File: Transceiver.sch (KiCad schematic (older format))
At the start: 31 parts

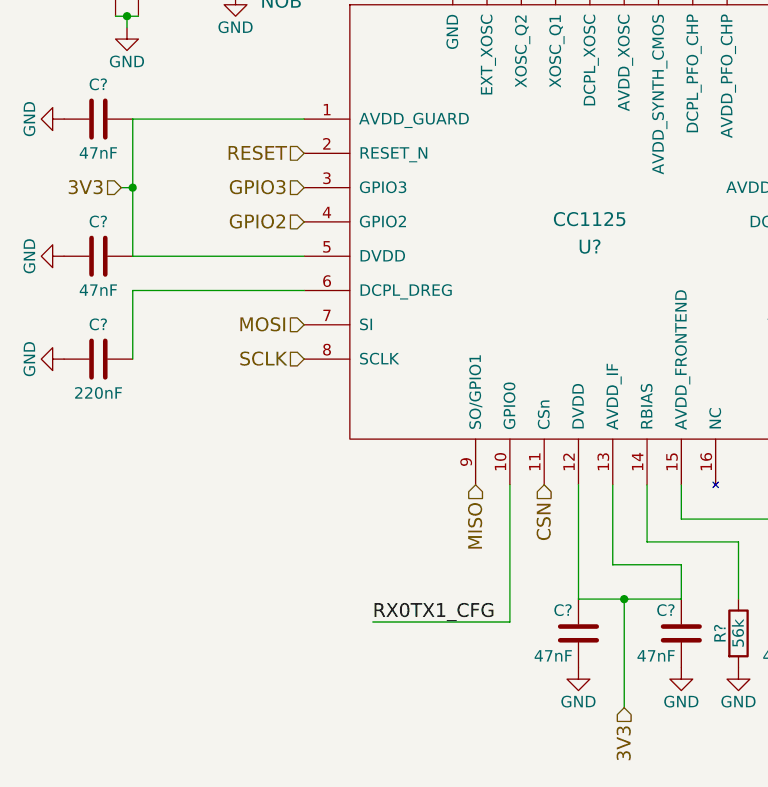
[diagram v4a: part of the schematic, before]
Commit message: added switches for various option and nmos array to control status leds
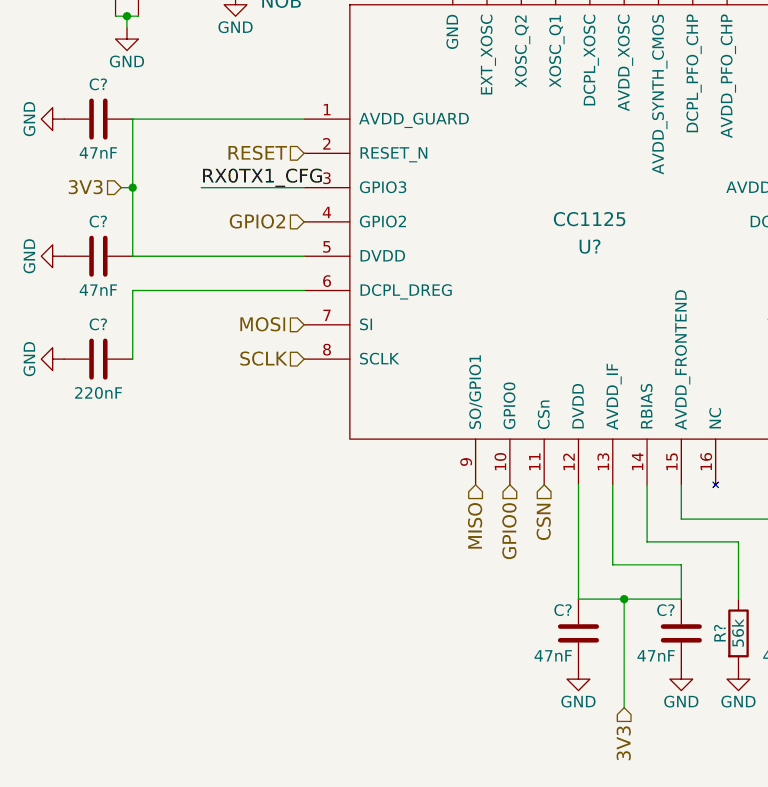
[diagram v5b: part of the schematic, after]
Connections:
- net GPIO3 is gone; now on net TRX_SIG: U?.3 (GPIO3)
- net TRX_SIG: no longer U?.10 (GPIO0)
- new net GPIO0: U?.10 (GPIO0)
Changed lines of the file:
@@
 Text HLabel 1800 3150 0    60   Input ~ 0
 RESET
-Text HLabel 1800 3300 0    60   Input ~ 0
-GPIO3
 Text HLabel 1800 3450 0    60   Input ~ 0
 GPIO2
@@
 Wire Wire Line
 	2350 1350 1850 1350
-Wire Wire Line
-	2700 4600 2700 5200
-Wire Wire Line
-	2700 5200 2100 5200
-Text Label 2100 5200 0    60   ~ 0
+Text Label 1350 3300 0    60   ~ 0
 RX0TX1_CFG
 Text Label 5750 1000 0    60   ~ 0
@@
 Text Label 7800 3200 0    60   ~ 0
 RX0TX1_CFG
+Text HLabel 2700 4600 3    60   Input ~ 0
+GPIO0
+Wire Wire Line
+	1800 3300 1350 3300
 $EndSCHEMATC

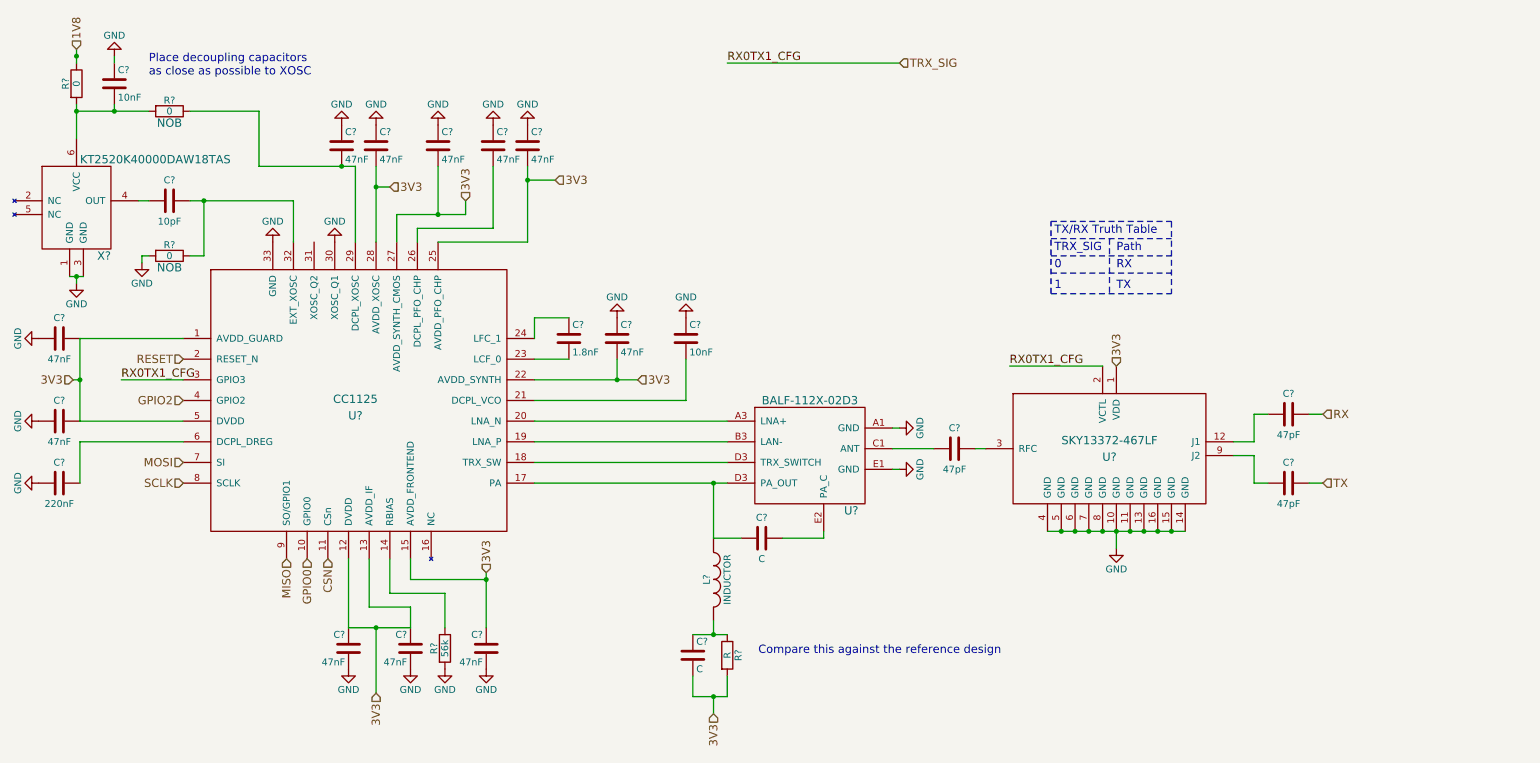
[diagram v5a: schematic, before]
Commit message: added a bunch of footprints and generated layout file
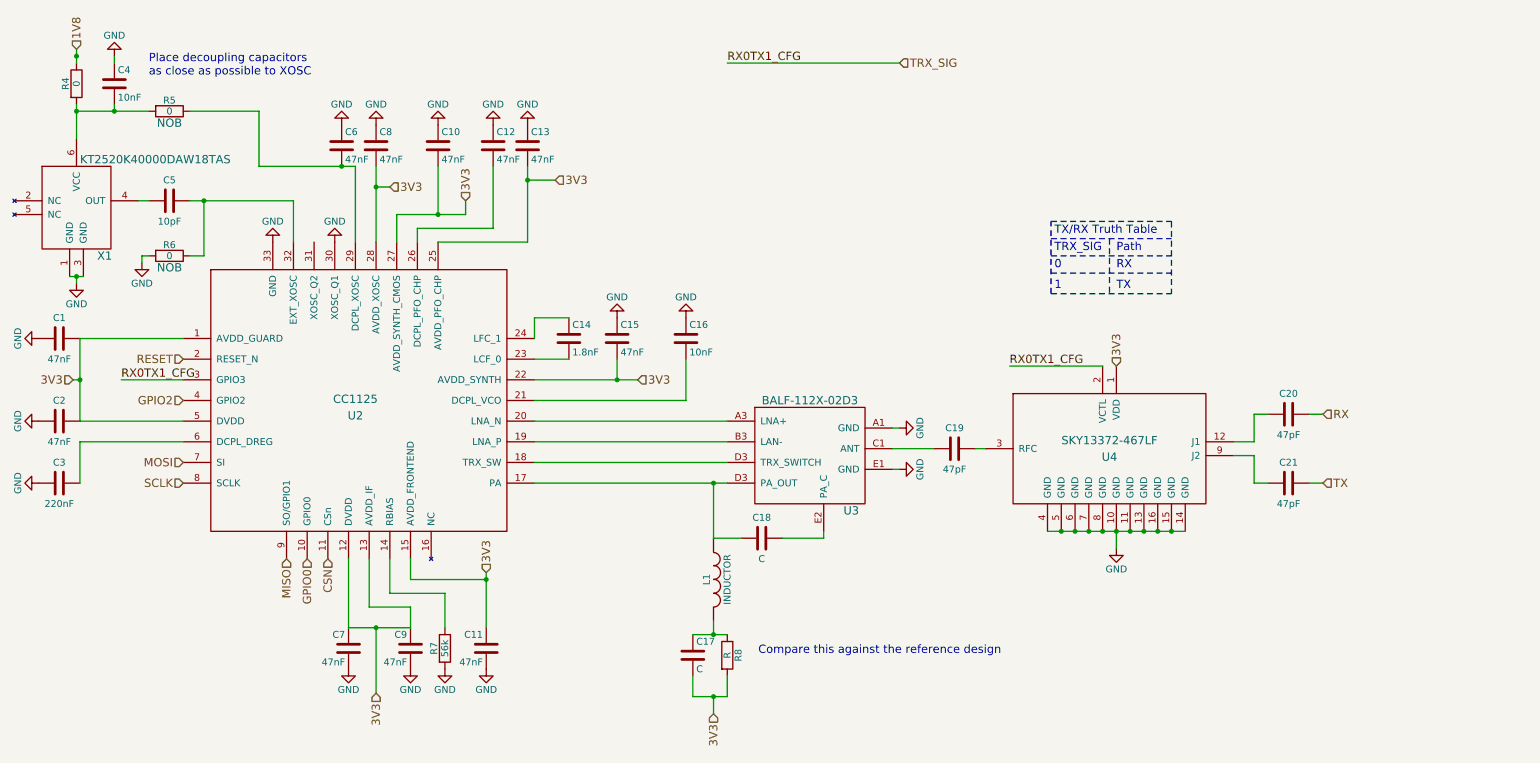
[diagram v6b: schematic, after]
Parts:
- C1, C10, C11, C12, C13, C15, C16, C2, C3, C4, C5, C6, C7, C8, C9: renamed from C?; footprint (none) -> Capacitors_SMD:C_0402
- R4, R5, R6, R7: renamed from R?; footprint (none) -> Resistors_SMD:R_0402
- U2: renamed from U?; footprint (none) -> SFUSat-Radio:PVQFN-N32
- U3: renamed from U?; footprint (none) -> SFUSat-Radio:CSPG_04
- U4: renamed from U?; footprint (none) -> SFUSat-Radio:QFN-16_650P
- X1: renamed from X?; footprint (none) -> SFUSat-Radio:DFN-6
- gave numbers to parts that had none: 8

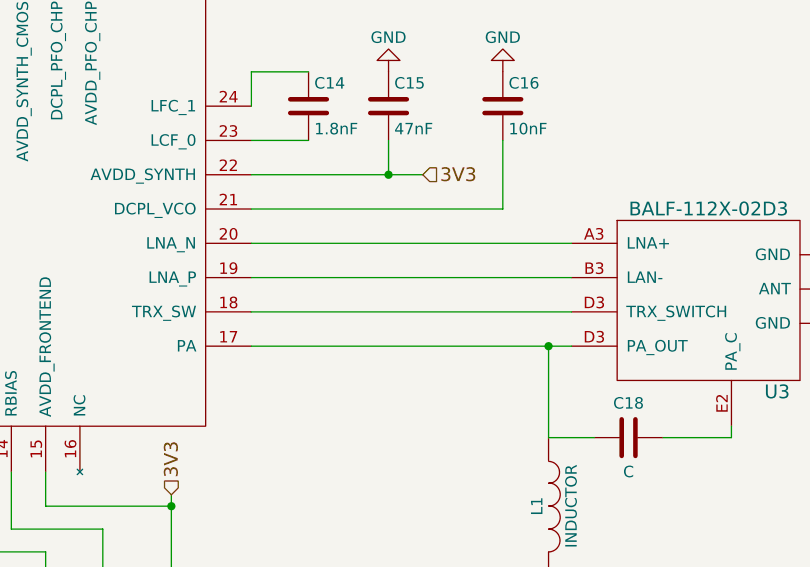
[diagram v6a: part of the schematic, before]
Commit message: setup netclasses and added more footprints
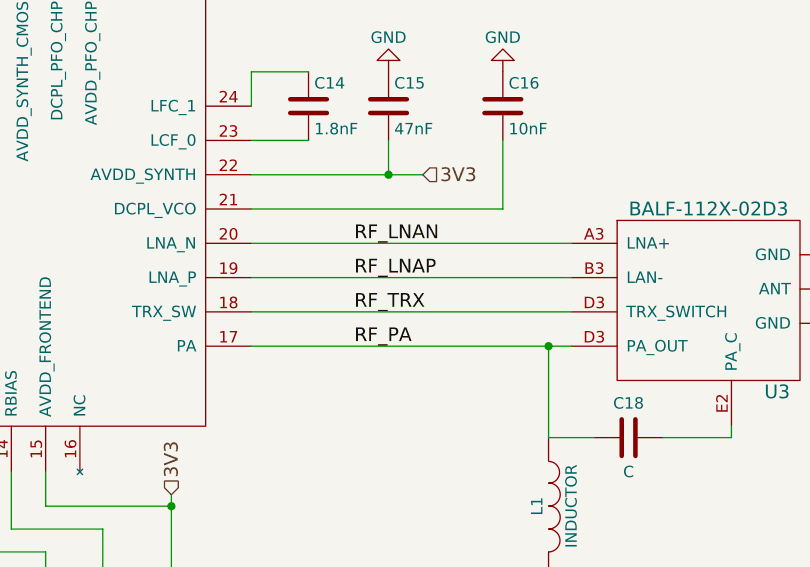
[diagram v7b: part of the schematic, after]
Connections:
- net RF_PA: now reaches C18.2, L1.1, U2.17 (PA), U3.D3 (TRX_SWITCH)
- net RF_TRX: now reaches U2.18 (TRX_SW), U3.D3 (TRX_SWITCH)
- net RF_LNAP: now reaches U2.19 (LNA_P), U3.B3 (LAN-)
- net RF_LNAN: now reaches U2.20 (LNA_N), U3.A3 (LNA+)
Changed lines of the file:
@@
 Wire Wire Line
 	1800 3300 1350 3300
+Text Label 4800 3600 0    60   ~ 0
+RF_LNAN
+Text Label 4800 3750 0    60   ~ 0
+RF_LNAP
+Text Label 4800 3900 0    60   ~ 0
+RF_TRX
+Text Label 4800 4050 0    60   ~ 0
+RF_PA
 $EndSCHEMATC
